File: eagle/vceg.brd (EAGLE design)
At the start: 100 x 80 mm, 64 parts, among them IC1 4052N, IC2 4001N, IC3 TL074P, IC5 CA3080E, Q1 2N3906INLINE, Q2 2N3906INLINE, U1 POWER

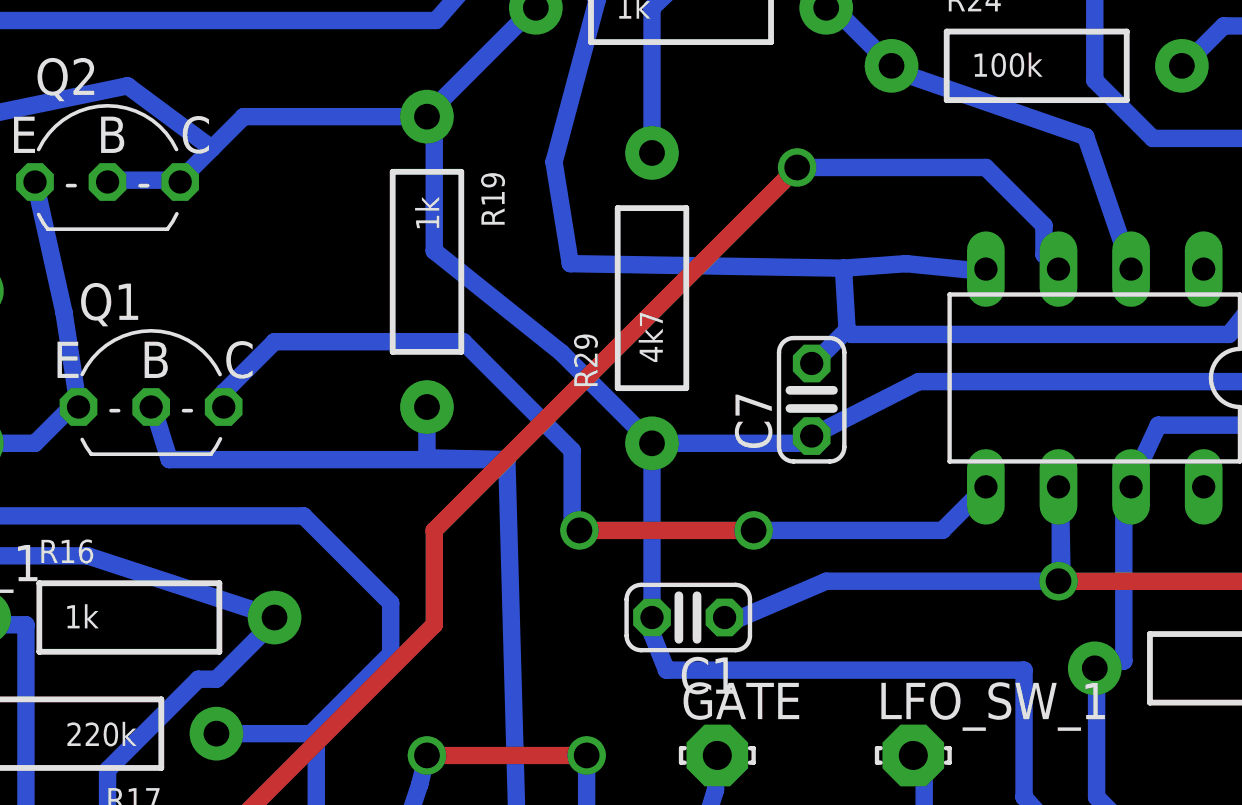
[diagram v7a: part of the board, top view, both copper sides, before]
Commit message: fixed schematic and board for 10k between 3906 and 3080
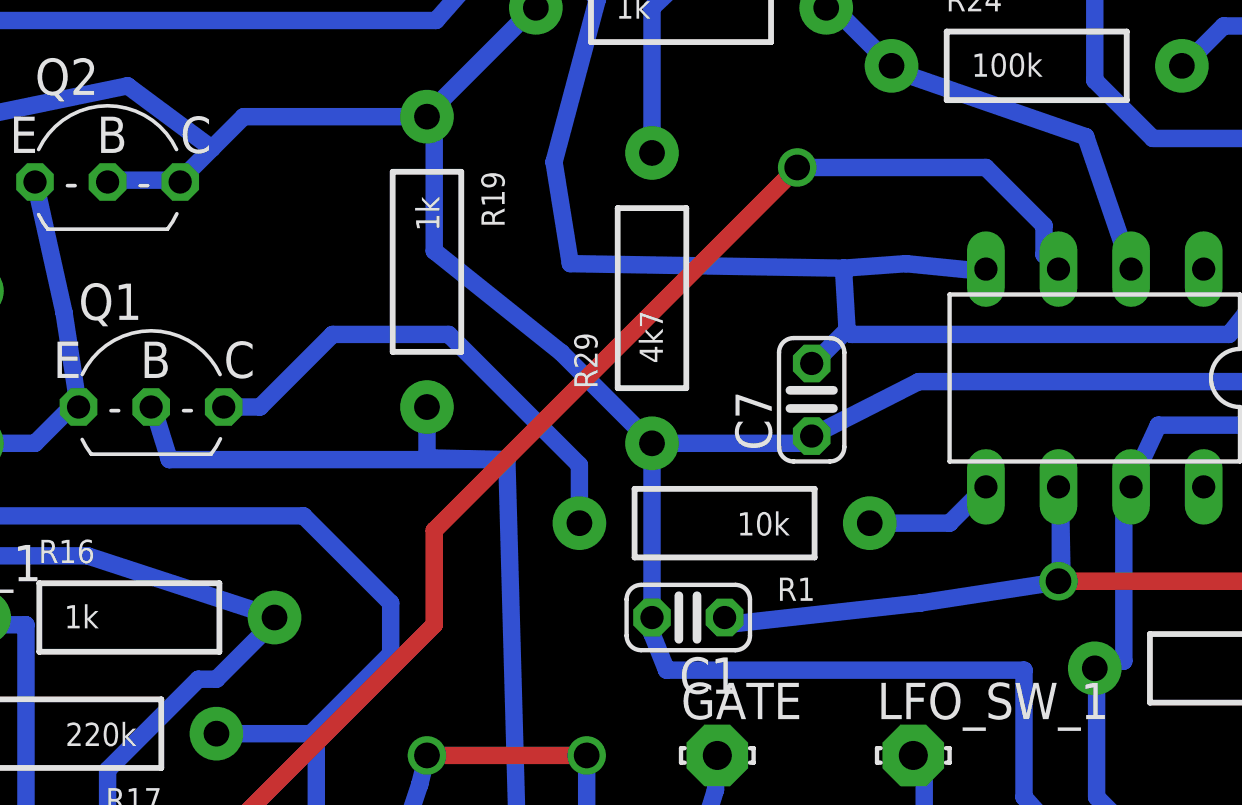
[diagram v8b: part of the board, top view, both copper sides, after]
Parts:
- added R1: 10k, SparkFun-Resistors:AXIAL-0.4
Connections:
- new net N$39: IC5.5, R1.P$1
- net N$21: now also R1.P$2; no longer IC5.5
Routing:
- net N$21: track 32.8 -> 17.4 mm, vias 2 -> 0
- net N$39: track 0.00 -> 4.59 mm
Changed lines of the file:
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@@
 <element name="TG_SWB_3" library="solpad" package="LSP10" value="LSP10" x="89.154" y="42.164"/>
 <element name="U1" library="eurorack" package="POWER_16" value="POWER" x="21.082" y="70.612"/>
+<element name="R1" library="SparkFun-Resistors" package="AXIAL-0.4" value="10k" x="45.72" y="49.276" rot="R180"/>
 </elements>
 <signals>
@@
 <contactref element="R23" pad="P$1"/>
 <contactref element="C1" pad="2"/>
-<contactref element="Q2" pad="C"/>
 <contactref element="Q2" pad="B"/>
 <contactref element="R25" pad="P$1"/>
@@
 <wire x1="27.78125" y1="62.38875" x2="26.67" y2="61.2775" width="0.6096" layer="16"/>
 <wire x1="35.2425" y1="63.5" x2="28.8925" y2="63.5" width="0.6096" layer="16"/>
-<wire x1="26.67" y1="61.2775" x2="26.67" y2="61.214" width="0.6096" layer="16"/>
 <wire x1="35.2425" y1="63.5" x2="39.0525" y2="67.31" width="0.6096" layer="16"/>
 <wire x1="39.0525" y1="67.31" x2="39.116" y2="67.31" width="0.6096" layer="16"/>
@@
 <wire x1="14.986" y1="62.5475" x2="14.986" y2="49.911" width="0.6096" layer="16"/>
 <wire x1="29.845" y1="46.0375" x2="29.972" y2="45.974" width="0.6096" layer="16"/>
+<contactref element="Q2" pad="C"/>
+<wire x1="26.67" y1="61.2775" x2="26.67" y2="61.214" width="0" layer="19" extent="16-16"/>
 </signal>
 <signal name="+12V">
@@
 <contactref element="C1" pad="1"/>
 <contactref element="IC5" pad="6"/>
-<wire x1="49.276" y1="47.244" x2="45.72" y2="45.72" width="0.6096" layer="16"/>
-<wire x1="57.531" y1="47.244" x2="49.276" y2="47.244" width="0.6096" layer="16"/>
+<wire x1="52.578" y1="46.482" x2="45.72" y2="45.72" width="0.6096" layer="16"/>
+<wire x1="57.531" y1="47.244" x2="52.578" y2="46.482" width="0.6096" layer="16"/>
 <wire x1="57.4675" y1="50.4825" x2="57.531" y2="47.244" width="0.6096" layer="16"/>
 <wire x1="45.72" y1="45.72" x2="45.72" y2="45.974" width="0.6096" layer="16"/>
@@
 <wire x1="77.1525" y1="64.4525" x2="77.216" y2="64.262" width="0.6096" layer="16"/>
 </signal>
-<signal name="N$21">
-<contactref element="Q1" pad="C"/>
-<contactref element="IC5" pad="5"/>
-<wire x1="28.194" y1="53.34" x2="28.194" y2="53.848" width="0.6096" layer="16"/>
-<wire x1="28.194" y1="53.848" x2="29.972" y2="55.626" width="0.6096" layer="16"/>
-<wire x1="29.972" y1="55.626" x2="36.576" y2="55.626" width="0.6096" layer="16"/>
-<wire x1="36.576" y1="55.626" x2="40.386" y2="51.816" width="0.6096" layer="16"/>
-<wire x1="40.386" y1="51.816" x2="40.386" y2="49.276" width="0.6096" layer="16"/>
-<wire x1="40.386" y1="49.276" x2="40.64" y2="49.022" width="0.6096" layer="16"/>
-<via x="40.64" y="49.022" extent="1-16" drill="0.9" shape="square"/>
-<wire x1="40.64" y1="49.022" x2="46.736" y2="49.022" width="0.6096" layer="1"/>
-<via x="46.736" y="49.022" extent="1-16" drill="0.9" shape="square"/>
-<wire x1="46.736" y1="49.022" x2="53.34" y2="49.022" width="0.6096" layer="16"/>
-<wire x1="53.34" y1="49.022" x2="54.864" y2="50.546" width="0.6096" layer="16"/>
-</signal>
 <signal name="N$41">
 <contactref element="IC5" pad="3"/>
@@
 <wire x1="52.2605" y1="41.2115" x2="52.324" y2="41.148" width="0.6096" layer="16"/>
 </signal>
+<signal name="N$21">
+<contactref element="Q1" pad="C"/>
+<contactref element="R1" pad="P$2"/>
+<wire x1="28.194" y1="53.34" x2="29.464" y2="53.34" width="0.6096" layer="16"/>
+<wire x1="29.464" y1="53.34" x2="32.004" y2="55.88" width="0.6096" layer="16"/>
+<wire x1="32.004" y1="55.88" x2="36.068" y2="55.88" width="0.6096" layer="16"/>
+<wire x1="36.068" y1="55.88" x2="40.64" y2="51.308" width="0.6096" layer="16"/>
+<wire x1="40.64" y1="51.308" x2="40.64" y2="49.276" width="0.6096" layer="16"/>
+</signal>
+<signal name="N$39">
+<contactref element="IC5" pad="5"/>
+<contactref element="R1" pad="P$1"/>
+<wire x1="50.8" y1="49.276" x2="53.594" y2="49.276" width="0.6096" layer="16"/>
+<wire x1="53.594" y1="49.276" x2="54.864" y2="50.546" width="0.6096" layer="16"/>
+</signal>
 </signals>
